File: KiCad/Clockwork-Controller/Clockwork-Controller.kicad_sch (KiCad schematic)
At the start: 96 parts, among them CN2 PJ-307N5, J1 DIN-6 male, J2 to DIN-6 Male, J3 Pause Button, J4 ICSP, J5 LED-Connector, Q1 AO3400A, Q2 SS8050, Q3 SS8050, Q4 SS8050, SW1 Guide/Follow, SW2 Mode -, SW3 Mode +, SW4 Frame -, SW5 Frame +, U1 ECS-TXO-3225MV-160-TR, U2 AP2210N-3.3TRG1, U3 74HCT14, U4 G3VM-61VY3(TR), U5 MCP4725, U6 LMC6482, U7 ATmega328P-A

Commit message: Renaming once more
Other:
- title: ImpulsWerk Controller -> Clockwork Controller
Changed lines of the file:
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@@
 	(paper "A3")
 	(title_block
-		(title "ImpulsWerk Controller")
+		(title "Clockwork Controller")
 		(date "2025-02-11")
 		(rev "Rev.A")

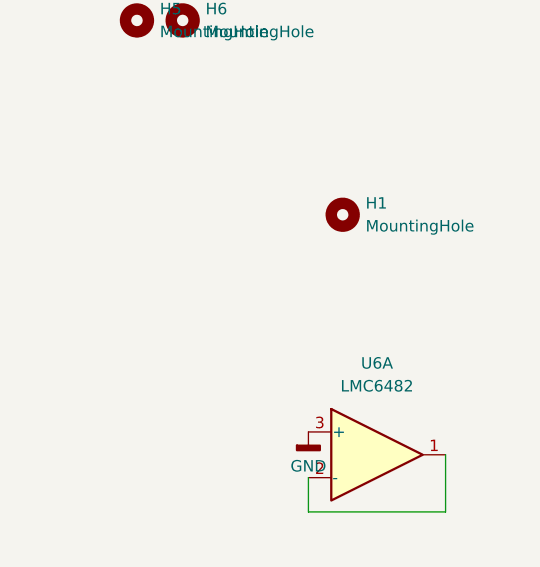
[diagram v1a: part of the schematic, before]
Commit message: New Gerbers, added the xtal to the BOM, new MH for OLED
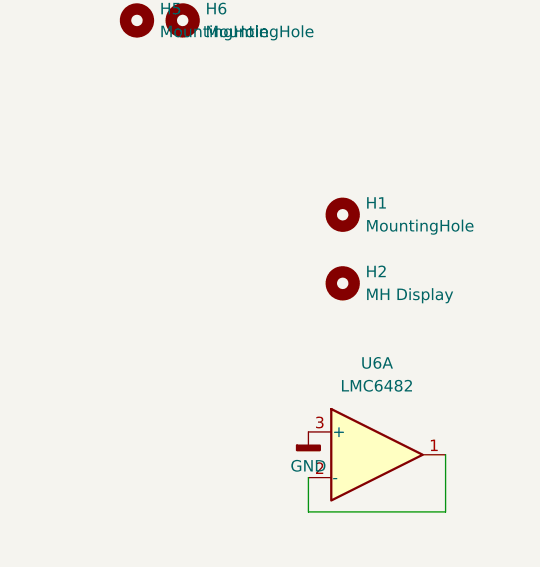
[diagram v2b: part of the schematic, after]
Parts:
- added H2: MH Display, MountingHole:MountingHole_2.2mm_M2_DIN965, symbol Mechanical:MountingHole
- U1: LCSC (none) -> C2442664; LCSC Part C2442664 -> (none)
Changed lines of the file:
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@@
 			)
 		)
-		(property "LCSC Part" "C2442664"
+		(property "LCSC Part" ""
 			(at 228.6 63.5 0)
+			(effects
+				(font
+					(size 1.27 1.27)
+				)
+				(hide yes)
+			)
+		)
+		(property "LCSC" "C2442664"
+			(at 228.6 52.07 0)
 			(effects
 				(font
@@
 					(unit 1)
 				)
+			)
+		)
+	)
+	(symbol
+		(lib_id "Mechanical:MountingHole")
+		(at 383.54 167.64 0)
+		(unit 1)
+		(exclude_from_sim yes)
+		(in_bom no)
+		(on_board yes)
+		(dnp no)
+		(fields_autoplaced yes)
+		(property "Reference" "H2"
+			(at 386.08 166.3699 0)
+			(effects
+				(font
+					(size 1.27 1.27)
+				)
+				(justify left)
+			)
+		)
+		(property "Value" "MH Display"
+			(at 386.08 168.9099 0)
+			(effects
+				(font
+					(size 1.27 1.27)
+				)
+				(justify left)
+			)
+		)
+		(property "Footprint" "MountingHole:MountingHole_2.2mm_M2_DIN965"
+			(at 383.54 167.64 0)
+			(effects
+				(font
+					(size 1.27 1.27)
+				)
+				(hide yes)
+			)
+		)
+		(property "Datasheet" "~"
+			(at 383.54 167.64 0)
+			(effects
+				(font
+					(size 1.27 1.27)
+				)
+				(hide yes)
+			)
+		)
+		(property "Description" "Mounting Hole without connection"
+			(at 383.54 167.64 0)
+			(effects
+				(font
+					(size 1.27 1.27)
+				)
+				(hide yes)
+			)
+		)
+		(instances
+			(project "Clockwork-Controller"
+				(path "/904e3c46-2ed3-4778-9ca9-733b218304b0"
+					(reference "H2")
+					(unit 1)
+				)

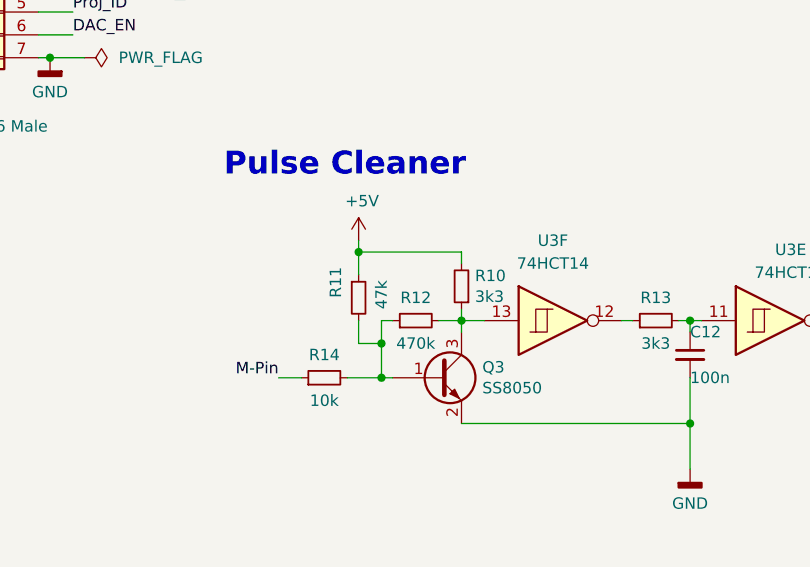
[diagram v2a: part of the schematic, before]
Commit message: Removing redundant R11, pulling M Pin up before reaching the Schmitt Triggers
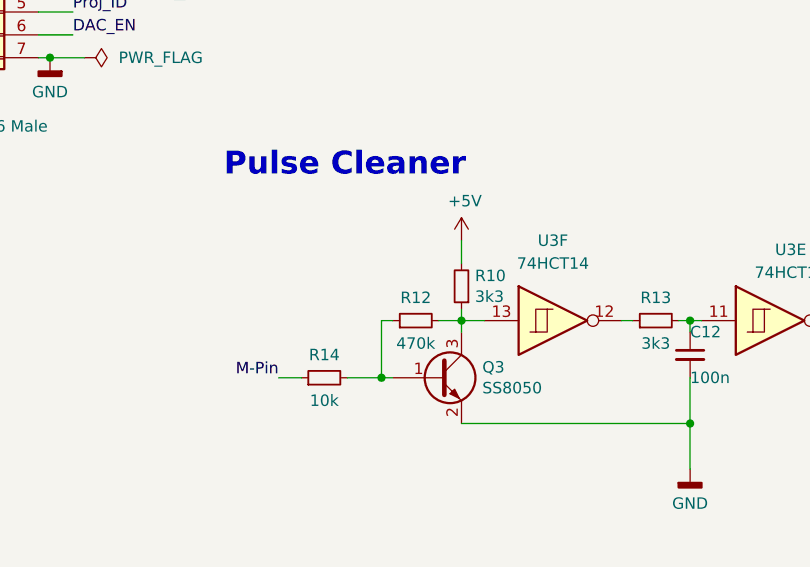
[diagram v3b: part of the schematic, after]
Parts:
- removed R11: 47k, Resistor_SMD:R_0603_1608Metric, symbol Device:R_Small
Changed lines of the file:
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@@
 	)
 	(junction
-		(at 114.3 115.57)
-		(diameter 0)
-		(color 0 0 0 0)
-	)
-	(junction
 		(at 220.98 184.15)
 		(diameter 0)
@@
 	)
 	(junction
-		(at 111.76 105.41)
-		(diameter 0)
-		(color 0 0 0 0)
-	)
-	(junction
 		(at 334.01 72.39)
 		(diameter 0)
@@
 	(wire
 		(pts
-			(xy 123.19 105.41) (xy 123.19 106.68)
+			(xy 123.19 104.14) (xy 123.19 106.68)
 		)
 		(stroke
@@
 	(wire
 		(pts
-			(xy 111.76 104.14) (xy 111.76 105.41)
-		)
-		(stroke
-			(width 0)
-			(type default)
-		)
-	)
-	(wire
-		(pts
 			(xy 223.52 111.76) (xy 222.25 111.76)
 		)
@@
 	(wire
 		(pts
-			(xy 114.3 113.03) (xy 114.3 115.57)
+			(xy 114.3 113.03) (xy 114.3 119.38)
 		)
 		(stroke
@@
 	(wire
 		(pts
-			(xy 111.76 113.03) (xy 111.76 115.57)
-		)
-		(stroke
-			(width 0)
-			(type default)
-		)
-	)
-	(wire
-		(pts
 			(xy 185.42 274.32) (xy 185.42 264.16)
 		)
@@
 	(wire
 		(pts
-			(xy 114.3 115.57) (xy 114.3 119.38)
-		)
-		(stroke
-			(width 0)
-			(type default)
-		)
-	)
-	(wire
-		(pts
 			(xy 87.63 207.01) (xy 88.9 207.01)
 		)
@@
 	(wire
 		(pts
-			(xy 111.76 105.41) (xy 123.19 105.41)
-		)
-		(stroke
-			(width 0)
-			(type default)
-		)
-	)
-	(wire
-		(pts
 			(xy 232.41 196.85) (xy 232.41 195.58)
 		)
@@
 	(wire
 		(pts
-			(xy 111.76 105.41) (xy 111.76 107.95)
-		)
-		(stroke
-			(width 0)
-			(type default)
-		)
-	)
-	(wire
-		(pts
 			(xy 243.84 189.23) (xy 243.84 193.04)
 		)
@@
 	(wire
 		(pts
-			(xy 111.76 115.57) (xy 114.3 115.57)
-		)
-		(stroke
-			(width 0)
-			(type default)
-		)
-	)
-	(wire
-		(pts
 			(xy 387.35 91.44) (xy 387.35 53.34)
 		)
@@
 	(symbol
 		(lib_id "power:+5V")
-		(at 111.76 104.14 0)
+		(at 123.19 104.14 0)
 		(unit 1)
 		(exclude_from_sim no)
@@
 		(dnp no)
 		(property "Reference" "#PWR013"
-			(at 111.76 107.95 0)
+			(at 123.19 107.95 0)
 			(effects
 				(font
@@
 		)
 		(property "Value" "+5V"
-			(at 112.141 99.7458 0)
+			(at 123.571 99.7458 0)
 			(effects
 				(font
@@
 		)
 		(property "Footprint" ""
-			(at 111.76 104.14 0)
+			(at 123.19 104.14 0)
 			(effects
 				(font
@@
 		)
 		(property "Datasheet" ""
-			(at 111.76 104.14 0)
+			(at 123.19 104.14 0)
 			(effects
 				(font
@@
 		)
 		(property "Description" "Power symbol creates a global label with name \"+5V\""
-			(at 111.76 104.14 0)
+			(at 123.19 104.14 0)
 			(effects
 				(font
@@
 					(unit 1)
 				)
-			)
-		)
-	)
-	(symbol
-		(lib_id "Device:R_Small")
-		(at 111.76 110.49 0)
-		(unit 1)
-		(exclude_from_sim no)
-		(in_bom yes)
-		(on_board yes)
-		(dnp no)
-		(property "Reference" "R11"
-			(at 109.22 110.49 90)
-			(effects
-				(font
-					(size 1.27 1.27)
-				)
-				(justify left)
-			)
-		)
-		(property "Value" "47k"
-			(at 114.3 111.76 90)
-			(effects
-				(font
-					(size 1.27 1.27)
-				)
-				(justify left)
-			)
-		)
-		(property "Footprint" "Resistor_SMD:R_0603_1608Metric"
-			(at 111.76 110.49 0)
-			(effects
-				(font
-					(size 1.27 1.27)
-				)
-				(hide yes)
-			)
-		)
-		(property "Datasheet" "https://www.lcsc.com/datasheet/lcsc_datasheet_2411221127_UNI-ROYAL-Uniroyal-Elec-0603WAF4702T5E_C25819.pdf"
-			(at 111.76 110.49 0)
-			(effects
-				(font
-					(size 1.27 1.27)
-				)
-				(hide yes)
-			)
-		)
-		(property "Description" ""
-			(at 111.76 110.49 0)
-			(effects
-				(font
-					(size 1.27 1.27)
-				)
-				(hide yes)
-			)
-		)
-		(property "LCSC" "C25819"
-			(at 111.76 110.49 0)
-			(effects
-				(font
-					(size 1.27 1.27)
-				)
-				(hide yes)
-			)
-		)
-		(pin "1"
-		)
-		(pin "2"
-		)
-		(instances
-			(project "SynCrystal-kicad"
-				(path "/904e3c46-2ed3-4778-9ca9-733b218304b0"
-					(reference "R11")
-					(unit 1)
-				)

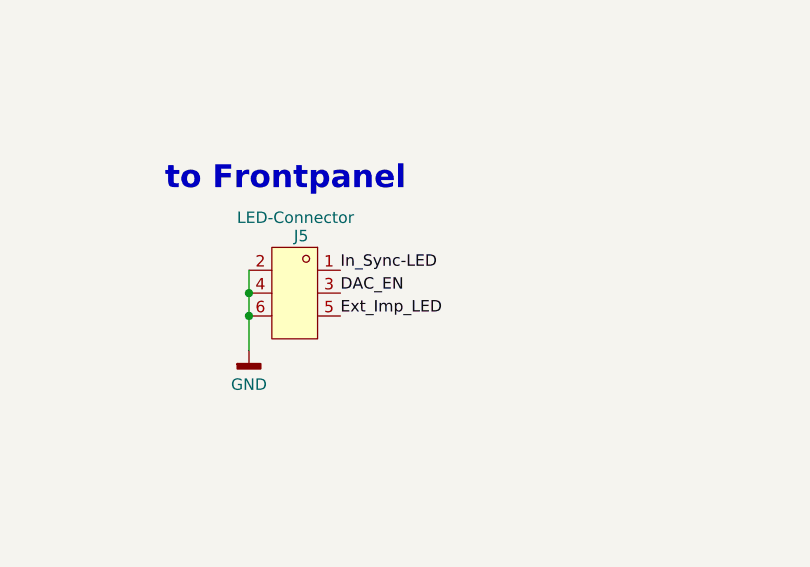
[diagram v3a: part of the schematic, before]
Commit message: Swao Ext.Imp and Sync LED
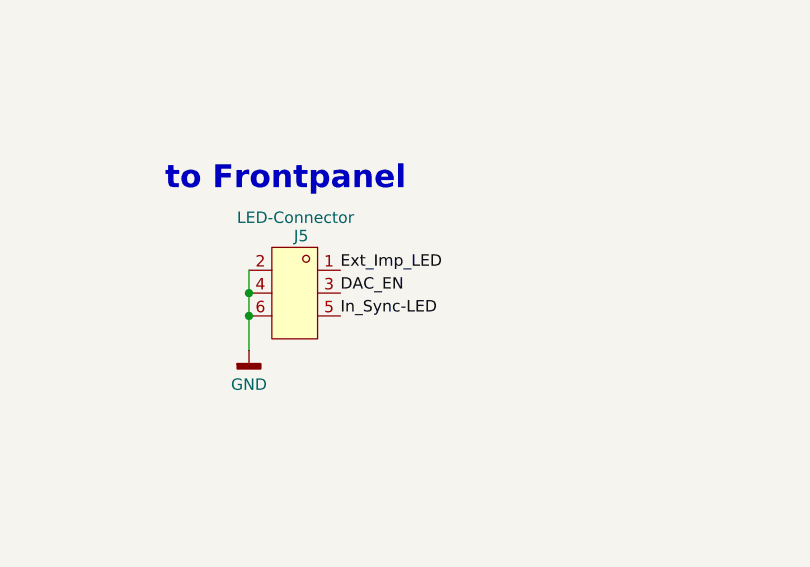
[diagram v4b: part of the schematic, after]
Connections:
- net Ext_Imp_LED: now also J5.1; no longer J5.5
- net In_Sync-LED: now also J5.5; no longer J5.1
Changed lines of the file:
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@@
 	)
 	(label "In_Sync-LED"
-		(at 283.21 240.03 0)
+		(at 283.21 245.11 0)
 		(effects
 			(font
@@
 	)
 	(label "Ext_Imp_LED"
-		(at 283.21 245.11 0)
+		(at 283.21 240.03 0)
 		(effects
 			(font

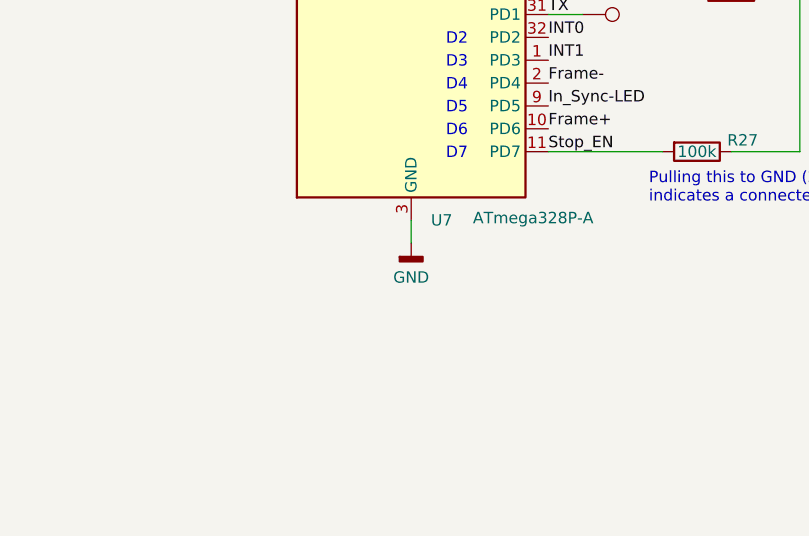
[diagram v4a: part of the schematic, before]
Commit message: Adding GND TPs
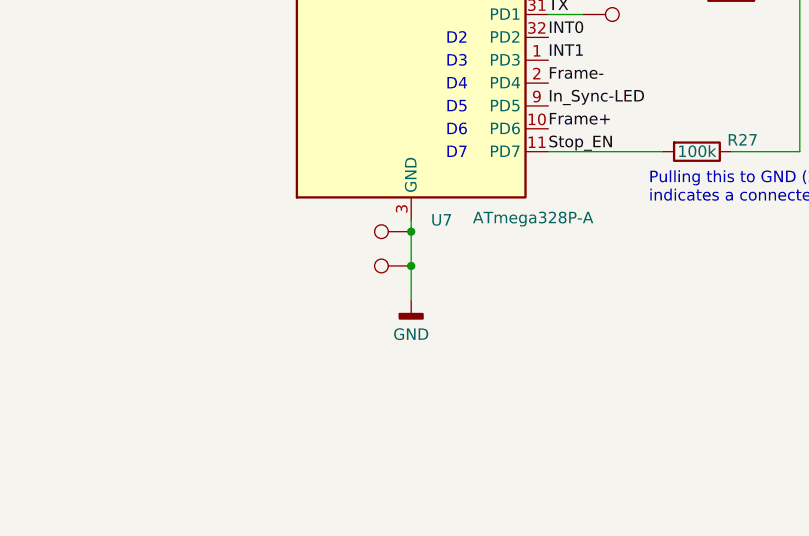
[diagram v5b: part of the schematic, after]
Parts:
- added TP3, TP4: GND, TestPoint:TestPoint_THTPad_1.5x1.5mm_Drill0.7mm, symbol Peacemans Teile:TestPoint_named
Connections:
- net GND: now also TP3.1, TP4.1
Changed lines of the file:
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@@
 	)
 	(junction
+		(at 63.5 246.38)
+		(diameter 0)
+		(color 0 0 0 0)
+	)
+	(junction
 		(at 340.36 35.56)
 		(diameter 0)
@@
 		(color 0 0 0 0)
 	)
+	(junction
+		(at 63.5 250.19)
+		(diameter 0)
+		(color 0 0 0 0)
+	)
 	(no_connect
 		(at 78.74 194.31)
@@
 	(wire
 		(pts
-			(xy 63.5 245.11) (xy 63.5 247.65)
+			(xy 63.5 245.11) (xy 63.5 246.38)
 		)
 		(stroke
@@
 	(wire
 		(pts
+			(xy 63.5 250.19) (xy 63.5 254)
+		)
+		(stroke
+			(width 0)
+			(type default)
+		)
+	)
+	(wire
+		(pts
 			(xy 300.99 186.69) (xy 299.72 186.69)
 		)
@@
 	(wire
 		(pts
+			(xy 63.5 246.38) (xy 63.5 250.19)
+		)
+		(stroke
+			(width 0)
+			(type default)
+		)
+	)
+	(wire
+		(pts
 			(xy 273.05 245.11) (xy 273.05 248.92)
 		)
@@
 	)
 	(symbol
+		(lib_id "Peacemans Teile:TestPoint_named")
+		(at 63.5 246.38 90)
+		(unit 1)
+		(exclude_from_sim no)
+		(in_bom yes)
+		(on_board yes)
+		(dnp no)
+		(fields_autoplaced yes)
+		(property "Reference" "TP3"
+			(at 56.642 246.38 0)
+			(effects
+				(font
+					(size 1.27 1.27)
+				)
+				(hide yes)
+			)
+		)
+		(property "Value" "GND"
+			(at 58.42 246.38 0)
+			(effects
+				(font
+					(size 1.27 1.27)
+				)
+				(hide yes)
+			)
+		)
+		(property "Footprint" "TestPoint:TestPoint_THTPad_1.5x1.5mm_Drill0.7mm"
+			(at 63.5 241.3 0)
+			(effects
+				(font
+					(size 1.27 1.27)
+				)
+				(hide yes)
+			)
+		)
+		(property "Datasheet" "~"
+			(at 63.5 241.3 0)
+			(effects
+				(font
+					(size 1.27 1.27)
+				)
+				(hide yes)
+			)
+		)
+		(property "Description" "test point"
+			(at 63.5 246.38 0)
+			(effects
+				(font
+					(size 1.27 1.27)
+				)
+				(hide yes)
+			)
+		)
+		(property "TP_Label" ""
+			(at 63.5 246.38 0)
+			(effects
+				(font
+					(size 1.27 1.27)
+				)
+			)
+		)
+		(pin "1"
+		)
+		(instances
+			(project "Clockwork-Controller"
+				(path "/904e3c46-2ed3-4778-9ca9-733b218304b0"
+					(reference "TP3")
+					(unit 1)
+				)
+			)
+		)
+	)
+	(symbol
 		(lib_id "Device:R_Small")
 		(at 251.46 195.58 270)
@@
 	)
 	(symbol
+		(lib_id "Peacemans Teile:TestPoint_named")
+		(at 63.5 250.19 90)
+		(unit 1)
+		(exclude_from_sim no)
+		(in_bom yes)
+		(on_board yes)
+		(dnp no)
+		(fields_autoplaced yes)
+		(property "Reference" "TP4"
+			(at 56.642 250.19 0)
+			(effects
+				(font
+					(size 1.27 1.27)
+				)
+				(hide yes)
+			)
+		)
+		(property "Value" "GND"
+			(at 58.42 250.19 0)
+			(effects
+				(font
+					(size 1.27 1.27)
+				)
+				(hide yes)
+			)
+		)
+		(property "Footprint" "TestPoint:TestPoint_THTPad_1.5x1.5mm_Drill0.7mm"
+			(at 63.5 245.11 0)
+			(effects
+				(font
+					(size 1.27 1.27)
+				)
+				(hide yes)
+			)
+		)
+		(property "Datasheet" "~"
+			(at 63.5 245.11 0)
+			(effects
+				(font
+					(size 1.27 1.27)
+				)
+				(hide yes)
+			)
+		)
+		(property "Description" "test point"
+			(at 63.5 250.19 0)
+			(effects
+				(font
+					(size 1.27 1.27)
+				)
+				(hide yes)
+			)
+		)
+		(property "TP_Label" ""
+			(at 63.5 250.19 0)
+			(effects
+				(font
+					(size 1.27 1.27)
+				)
+			)
+		)
+		(pin "1"
+		)
+		(instances
+			(project "Clockwork-Controller"
+				(path "/904e3c46-2ed3-4778-9ca9-733b218304b0"
+					(reference "TP4")
+					(unit 1)
+				)
+			)
+		)
+	)
+	(symbol
 		(lib_id "Device:R")
 		(at 99.06 214.63 270)
@@
 	(symbol
 		(lib_id "power:GNDD")
-		(at 63.5 247.65 0)
+		(at 63.5 254 0)
 		(unit 1)
 		(exclude_from_sim no)
@@
 		(dnp no)
 		(property "Reference" "#PWR042"
-			(at 63.5 254 0)
+			(at 63.5 260.35 0)
 			(effects
 				(font
@@
 		)
 		(property "Value" "GND"
-			(at 63.5 251.46 0)
+			(at 63.5 257.81 0)
 			(effects
 				(font
@@
 		)
 		(property "Footprint" ""
-			(at 63.5 247.65 0)
+			(at 63.5 254 0)
 			(effects
 				(font
@@
 		)
 		(property "Datasheet" ""
-			(at 63.5 247.65 0)
+			(at 63.5 254 0)
 			(effects
 				(font
@@
 		)
 		(property "Description" "Power symbol creates a global label with name \"GNDD\" , digital ground"
-			(at 63.5 247.65 0)
+			(at 63.5 254 0)
 			(effects
 				(font

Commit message: Moving the 3.5mm jack inwards to be flush with the edge
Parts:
- H1: footprint Peacemans Teile:Kabelbinder 3mm -> Peacemans Teile:Kabelbinder 4mm
- SW2, SW3, SW4, SW5: LCSC Part C93156 -> (none)
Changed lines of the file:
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@@
 			)
 		)
-		(property "LCSC Part" "C93156"
+		(property "LCSC Part" ""
 			(at 231.14 255.27 0)
 			(effects
@@
 			)
 		)
-		(property "LCSC Part" "C93156"
+		(property "LCSC Part" ""
 			(at 231.14 273.05 0)
 			(effects
@@
 			)
 		)
-		(property "LCSC Part" "C93156"
+		(property "LCSC Part" ""
 			(at 231.14 281.94 0)
 			(effects
@@
 			)
 		)
-		(property "Footprint" "Peacemans Teile:Kabelbinder 3mm"
+		(property "Footprint" "Peacemans Teile:Kabelbinder 4mm"
 			(at 383.54 160.02 0)
 			(effects
@@
 			)
 		)
-		(property "LCSC Part" "C93156"
+		(property "LCSC Part" ""
 			(at 231.14 264.16 0)
 			(effects

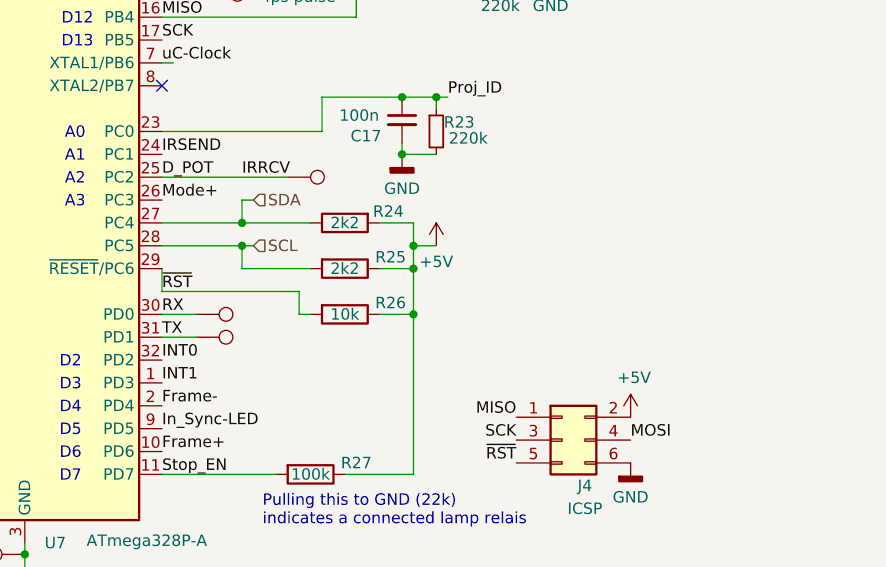
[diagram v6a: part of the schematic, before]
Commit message: Adding FTDI port
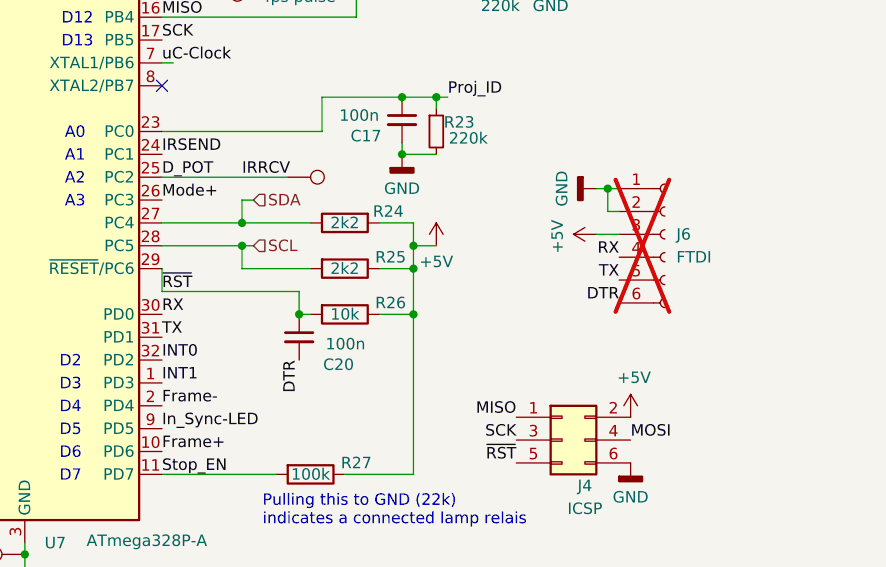
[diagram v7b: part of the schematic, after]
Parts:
- removed TP12: Rx, TestPoint:TestPoint_THTPad_1.5x1.5mm_Drill0.7mm, symbol Peacemans Teile:TestPoint_named
- removed TP13: Tx, TestPoint:TestPoint_THTPad_1.5x1.5mm_Drill0.7mm, symbol Peacemans Teile:TestPoint_named
- added C20: 100n, Capacitor_SMD:C_0603_1608Metric, symbol Device:C_Small
- added J6: FTDI, Connector_PinHeader_2.54mm:PinHeader_1x06_P2.54mm_Vertical, symbol Connector:Conn_01x06_Socket
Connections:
- net +5V: now also J6.3 (Pin_3)
- net GND: now also J6.1 (Pin_1), J6.2 (Pin_2)
- net RX: now also J6.4 (Pin_4)
- net TX: now also J6.5 (Pin_5)
- net ~{RST}: now also C20.1
- new net DTR: C20.2, J6.6 (Pin_6)
